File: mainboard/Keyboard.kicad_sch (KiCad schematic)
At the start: 111 parts, among them J10 Cassette, J11 Joystick, J12 Keyboard, Q3 TIS92, Q4 TIS92, Q5 TIS92, Q6 TIS92, Q7 TIS92, Q8 TIS92, Q9 TIS92, U40 TMS9901, U41 RC4558, U42 74LS156, U43 TIL119, U44 TIL119

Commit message: PCB routed
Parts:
- L13, L14, L15, L16, L17, L18, L19, L20, L21, L22: footprint Resistor_THT:R_Axial_DIN0207_L6.3mm_D2.5mm_P15.24mm_Horizontal -> Resistor_THT:R_Axial_DIN0207_L6.3mm_D2.5mm_P7.62mm_Horizontal
- Q3, Q4, Q5, Q6, Q7, Q8, Q9: footprint (none) -> Package_TO_SOT_THT:TO-92_HandSolder
- U39: renamed from U40; footprint Package_DIP:DIP-40_W15.24mm_LongPads -> Package_DIP:DIP-40_W15.24mm_Socket_LongPads
- U40: renamed from U41; footprint Package_DIP:DIP-8_W7.62mm_LongPads -> Package_DIP:DIP-8_W7.62mm_Socket_LongPads
- U41: renamed from U42; footprint Package_DIP:DIP-16_W7.62mm_LongPads -> Package_DIP:DIP-16_W7.62mm_Socket_LongPads
- U42: renamed from U43; footprint (none) -> Package_DIP:DIP-6_W7.62mm_Socket_LongPads
- U43: renamed from U44; footprint (none) -> Package_DIP:DIP-6_W7.62mm_Socket_LongPads
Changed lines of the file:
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@@
   (symbol (lib_id "TI-Customs:TMS9901") (at 69.85 86.36 0) (unit 1)
     (in_bom yes) (on_board yes)
-    (property "Reference" "U40" (id 0) (at 81.28 57.15 0)
+    (property "Reference" "U39" (id 0) (at 81.28 57.15 0)
       (effects (font (size 1.524 1.524)) (justify right))
     )
@@
       (effects (font (size 1.524 1.524)))
     )
-    (property "Footprint" "Package_DIP:DIP-40_W15.24mm_LongPads" (id 2) (at 69.85 86.36 0)
+    (property "Footprint" "Package_DIP:DIP-40_W15.24mm_Socket_LongPads" (id 2) (at 69.85 86.36 0)
       (effects (font (size 1.524 1.524)) hide)
     )
@@
       (effects (font (size 1.27 1.27)) (justify left))
     )
-    (property "Footprint" "" (id 2) (at 189.23 53.975 0)
+    (property "Footprint" "Package_TO_SOT_THT:TO-92_HandSolder" (id 2) (at 189.23 53.975 0)
       (effects (font (size 1.27 1.27) italic) (justify left) hide)
     )
@@
   (symbol (lib_id "Console-rescue:TIL111") (at 210.82 52.07 0) (unit 1)
     (in_bom yes) (on_board yes)
-    (property "Reference" "U44" (id 0) (at 210.82 49.53 0)
+    (property "Reference" "U43" (id 0) (at 210.82 49.53 0)
       (effects (font (size 1.778 1.778)))
     )
@@
       (effects (font (size 1.778 1.778)))
     )
-    (property "Footprint" "" (id 2) (at 210.82 52.07 0)
+    (property "Footprint" "Package_DIP:DIP-6_W7.62mm_Socket_LongPads" (id 2) (at 210.82 52.07 0)
       (effects (font (size 1.524 1.524)) hide)
     )
@@
       (effects (font (size 1.27 1.27)) (justify left))
     )
-    (property "Footprint" "" (id 2) (at 231.14 53.975 0)
+    (property "Footprint" "Package_TO_SOT_THT:TO-92_HandSolder" (id 2) (at 231.14 53.975 0)
       (effects (font (size 1.27 1.27) italic) (justify left) hide)
     )
@@
       (effects (font (size 1.27 1.27)) (justify left))
     )
-    (property "Footprint" "" (id 2) (at 189.23 36.195 0)
+    (property "Footprint" "Package_TO_SOT_THT:TO-92_HandSolder" (id 2) (at 189.23 36.195 0)
       (effects (font (size 1.27 1.27) italic) (justify left) hide)
     )
@@
   (symbol (lib_id "Console-rescue:TIL111") (at 210.82 34.29 0) (unit 1)
     (in_bom yes) (on_board yes)
-    (property "Reference" "U43" (id 0) (at 210.82 31.75 0)
+    (property "Reference" "U42" (id 0) (at 210.82 31.75 0)
       (effects (font (size 1.778 1.778)))
     )
@@
       (effects (font (size 1.778 1.778)))
     )
-    (property "Footprint" "" (id 2) (at 210.82 34.29 0)
+    (property "Footprint" "Package_DIP:DIP-6_W7.62mm_Socket_LongPads" (id 2) (at 210.82 34.29 0)
       (effects (font (size 1.524 1.524)) hide)
     )
@@
       (effects (font (size 1.27 1.27)) (justify left))
     )
-    (property "Footprint" "" (id 2) (at 231.14 36.195 0)
+    (property "Footprint" "Package_TO_SOT_THT:TO-92_HandSolder" (id 2) (at 231.14 36.195 0)
       (effects (font (size 1.27 1.27) italic) (justify left) hide)
     )
@@
       (effects (font (size 1.27 1.27)) (justify left))
     )
-    (property "Footprint" "Resistor_THT:R_Axial_DIN0207_L6.3mm_D2.5mm_P15.24mm_Horizontal" (id 2) (at 245.11 49.53 0)
+    (property "Footprint" "Resistor_THT:R_Axial_DIN0207_L6.3mm_D2.5mm_P7.62mm_Horizontal" (id 2) (at 245.11 49.53 0)
       (effects (font (size 1.524 1.524)) hide)
     )
@@
       (effects (font (size 1.27 1.27)) (justify left))
     )
-    (property "Footprint" "Resistor_THT:R_Axial_DIN0207_L6.3mm_D2.5mm_P15.24mm_Horizontal" (id 2) (at 245.11 31.75 0)
+    (property "Footprint" "Resistor_THT:R_Axial_DIN0207_L6.3mm_D2.5mm_P7.62mm_Horizontal" (id 2) (at 245.11 31.75 0)
       (effects (font (size 1.524 1.524)) hide)
     )
@@
       (effects (font (size 1.27 1.27)) (justify left))
     )
-    (property "Footprint" "Resistor_THT:R_Axial_DIN0207_L6.3mm_D2.5mm_P15.24mm_Horizontal" (id 2) (at 231.14 20.32 0)
+    (property "Footprint" "Resistor_THT:R_Axial_DIN0207_L6.3mm_D2.5mm_P7.62mm_Horizontal" (id 2) (at 231.14 20.32 0)
       (effects (font (size 1.524 1.524)) hide)
     )
@@
       (effects (font (size 1.27 1.27)) (justify left))
     )
-    (property "Footprint" "Resistor_THT:R_Axial_DIN0207_L6.3mm_D2.5mm_P15.24mm_Horizontal" (id 2) (at 240.03 22.86 0)
+    (property "Footprint" "Resistor_THT:R_Axial_DIN0207_L6.3mm_D2.5mm_P7.62mm_Horizontal" (id 2) (at 240.03 22.86 0)
       (effects (font (size 1.524 1.524)) hide)
     )
@@
   (symbol (lib_id "74xx:74LS156") (at 115.57 149.86 0) (unit 1)
     (in_bom yes) (on_board yes)
-    (property "Reference" "U42" (id 0) (at 114.3 146.05 0)
+    (property "Reference" "U41" (id 0) (at 114.3 146.05 0)
       (effects (font (size 1.524 1.524)))
     )
@@
       (effects (font (size 1.524 1.524)))
     )
-    (property "Footprint" "Package_DIP:DIP-16_W7.62mm_LongPads" (id 2) (at 115.57 149.86 0)
+    (property "Footprint" "Package_DIP:DIP-16_W7.62mm_Socket_LongPads" (id 2) (at 115.57 149.86 0)
       (effects (font (size 1.524 1.524)) hide)
     )
@@
       (effects (font (size 1.27 1.27)) (justify left))
     )
-    (property "Footprint" "" (id 2) (at 154.94 53.975 0)
+    (property "Footprint" "Package_TO_SOT_THT:TO-92_HandSolder" (id 2) (at 154.94 53.975 0)
       (effects (font (size 1.27 1.27) italic) (justify left) hide)
     )
@@
     )
     (property "Value" "6.8µH" (id 1) (at 154.94 140.97 90))
-    (property "Footprint" "Resistor_THT:R_Axial_DIN0207_L6.3mm_D2.5mm_P15.24mm_Horizontal" (id 2) (at 154.94 139.7 0)
+    (property "Footprint" "Resistor_THT:R_Axial_DIN0207_L6.3mm_D2.5mm_P7.62mm_Horizontal" (id 2) (at 154.94 139.7 0)
       (effects (font (size 1.524 1.524)) hide)
     )
@@
     )
     (property "Value" "6.8µH" (id 1) (at 167.64 143.51 90))
-    (property "Footprint" "Resistor_THT:R_Axial_DIN0207_L6.3mm_D2.5mm_P15.24mm_Horizontal" (id 2) (at 167.64 142.24 0)
+    (property "Footprint" "Resistor_THT:R_Axial_DIN0207_L6.3mm_D2.5mm_P7.62mm_Horizontal" (id 2) (at 167.64 142.24 0)
       (effects (font (size 1.524 1.524)) hide)
     )
@@
     )
     (property "Value" "6.8µH" (id 1) (at 154.94 153.67 90))
-    (property "Footprint" "Resistor_THT:R_Axial_DIN0207_L6.3mm_D2.5mm_P15.24mm_Horizontal" (id 2) (at 154.94 152.4 0)
+    (property "Footprint" "Resistor_THT:R_Axial_DIN0207_L6.3mm_D2.5mm_P7.62mm_Horizontal" (id 2) (at 154.94 152.4 0)
       (effects (font (size 1.524 1.524)) hide)
     )
@@
     )
     (property "Value" "6.8µH" (id 1) (at 167.64 156.21 90))
-    (property "Footprint" "Resistor_THT:R_Axial_DIN0207_L6.3mm_D2.5mm_P15.24mm_Horizontal" (id 2) (at 167.64 154.94 0)
+    (property "Footprint" "Resistor_THT:R_Axial_DIN0207_L6.3mm_D2.5mm_P7.62mm_Horizontal" (id 2) (at 167.64 154.94 0)
       (effects (font (size 1.524 1.524)) hide)
     )
@@
     )
     (property "Value" "6.8µH" (id 1) (at 180.34 158.75 90))
-    (property "Footprint" "Resistor_THT:R_Axial_DIN0207_L6.3mm_D2.5mm_P15.24mm_Horizontal" (id 2) (at 180.34 157.48 0)
+    (property "Footprint" "Resistor_THT:R_Axial_DIN0207_L6.3mm_D2.5mm_P7.62mm_Horizontal" (id 2) (at 180.34 157.48 0)
       (effects (font (size 1.524 1.524)) hide)
     )
@@
     )
     (property "Value" "6.8µH" (id 1) (at 193.04 161.29 90))
-    (property "Footprint" "Resistor_THT:R_Axial_DIN0207_L6.3mm_D2.5mm_P15.24mm_Horizontal" (id 2) (at 193.04 160.02 0)
+    (property "Footprint" "Resistor_THT:R_Axial_DIN0207_L6.3mm_D2.5mm_P7.62mm_Horizontal" (id 2) (at 193.04 160.02 0)
       (effects (font (size 1.524 1.524)) hide)
     )
@@
       (effects (font (size 1.27 1.27)) (justify left))
     )
-    (property "Footprint" "" (id 2) (at 207.01 118.745 0)
+    (property "Footprint" "Package_TO_SOT_THT:TO-92_HandSolder" (id 2) (at 207.01 118.745 0)
       (effects (font (size 1.27 1.27) italic) (justify left) hide)
     )
@@
       (effects (font (size 1.27 1.27)) (justify left))
     )
-    (property "Footprint" "" (id 2) (at 180.34 118.745 0)
+    (property "Footprint" "Package_TO_SOT_THT:TO-92_HandSolder" (id 2) (at 180.34 118.745 0)
       (effects (font (size 1.27 1.27) italic) (justify left) hide)
     )
@@
   (symbol (lib_id "Console-rescue:LM358") (at 135.89 33.02 180) (unit 2)
     (in_bom yes) (on_board yes)
-    (property "Reference" "U41" (id 0) (at 135.89 33.02 0)
+    (property "Reference" "U40" (id 0) (at 135.89 33.02 0)
       (effects (font (size 1.524 1.524)))
     )
@@
       (effects (font (size 1.524 1.524)) (justify right))
     )
-    (property "Footprint" "Package_DIP:DIP-8_W7.62mm_LongPads" (id 2) (at 135.89 33.02 0)
+    (property "Footprint" "Package_DIP:DIP-8_W7.62mm_Socket_LongPads" (id 2) (at 135.89 33.02 0)
       (effects (font (size 1.524 1.524)) hide)
     )
@@
   (symbol (lib_id "Console-rescue:LM358") (at 115.57 43.18 0) (mirror y) (unit 1)
     (in_bom yes) (on_board yes)
-    (property "Reference" "U41" (id 0) (at 115.57 43.18 0)
+    (property "Reference" "U40" (id 0) (at 115.57 43.18 0)
       (effects (font (size 1.524 1.524)))
     )
@@
       (effects (font (size 1.524 1.524)) (justify right))
     )
-    (property "Footprint" "Package_DIP:DIP-8_W7.62mm_LongPads" (id 2) (at 115.57 43.18 0)
-      (effects (font (size 1.524 1.524)) hide)
-    )
+    (property "Footprint" "Package_DIP:DIP-8_W7.62mm_Socket_LongPads" (id 2) (at 115.57 43.18 0)
+      (effects (font (size 1.524 1.524)) hide)
+    )

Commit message: unicorn work
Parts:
- removed J12: Keyboard, Connector_PinHeader_2.54mm:PinHeader_1x15_P2.54mm_Vertical, symbol Console-rescue:CONN_01X15
- added J12: Keyboard, symbol Connector_Generic:Conn_01x18
- renumbered C62 to C54, C63 to C55, C64 to C56, C65 to C57, C66 to C58, C67 to C59, C68 to C60, C69 to C61, C70 to C62, C71 to C63, C72 to C64, C73 to C65, C74 to C66, C75 to C67, C76 to C68, C77 to C69, C78 to C70, C79 to C71, C80 to C72, C81 to C73, C82 to C74, C83 to C75, C84 to C76, C85 to C77, C86 to C78, C87 to C79, C88 to C80, C89 to C81, C90 to C82, C91 to C83, C92 to C84, C93 to C85, C94 to C86, C95 to C87, C96 to C88, R39 to R35, R40 to R36, R41 to R37, R42 to R38, R43 to R39, R44 to R40, R45 to R41, R46 to R42, R47 to R43, R48 to R44, R49 to R45, R50 to R46, R51 to R47, R52 to R48, R53 to R49, R54 to R50, R55 to R51, R56 to R52, R57 to R53, R58 to R54, R59 to R55, R60 to R56, R61 to R57, R62 to R58, R63 to R59, R64 to R60, R65 to R61, R66 to R62, R67 to R63, R68 to R64, R69 to R65, R70 to R66, R71 to R67, R72 to R68, R73 to R69, R74 to R70, R75 to R71, R76 to R72, R77 to R73, R78 to R74, R79 to R75, R80 to R76, R81 to R77, R82 to R78, R83 to R79, R84 to R80, R85 to R81, R86 to R82, R87 to R83, R88 to R84, U39 to U35, U40 to U36, U41 to U37, U42 to U38, U43 to U39
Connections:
- net +5V: now also J12.17 (Pin_17)
- net GND: now also J12.16 (Pin_16)
- net ~{RESET}: now also J12.18 (Pin_18)
- net at L13.2: now also J12.9 (Pin_9)
- net at L15.2: now also J12.8 (Pin_8)
- net at L14.2: now also J12.12 (Pin_12)
- net at L16.2: now also J12.13 (Pin_13)
- net at L17.2: now also J12.14 (Pin_14)
- net at L18.2: now also J12.15 (Pin_15)
- net at J11.9, R68.1: now also J12.1 (Pin_1)
- net at R78.1: now also J12.10 (Pin_10)
- net at R80.1: now also J12.11 (Pin_11)
- net at J11.8, R70.1: now also J12.2 (Pin_2)
- net at R76.1: now also J12.3 (Pin_3)
- net at J11.5, R66.1: now also J12.4 (Pin_4)
- net at J11.4, R64.1: now also J12.5 (Pin_5)
- net at R83.1: now also J12.6 (Pin_6)
- net at J11.3, R72.1: now also J12.7 (Pin_7)
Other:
- moved on the sheet: C54, C55, C56, C57, C58, C59, C60, C61, C62, C63, C64, C65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

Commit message: unicorn work
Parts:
- J12: footprint (none) -> Connector_PinHeader_2.54mm:PinHeader_1x18_P2.54mm_Vertical
- renumbered C54 to C62, C55 to C63, C56 to C64, C57 to C65, C58 to C66, C59 to C67, C60 to C68, C61 to C69, C62 to C70, C63 to C71, C64 to C72, C65 to C73, C66 to C74, C67 to C75, C68 to C76, C69 to C77, C70 to C78, C71 to C79, C72 to C80, C73 to C81, C74 to C82, C75 to C83, C76 to C84, C77 to C85, C78 to C86, C79 to C87, C80 to C88, C81 to C89, C82 to C90, C83 to C91, C84 to C92, C85 to C93, C86 to C94, C87 to C95, C88 to C96

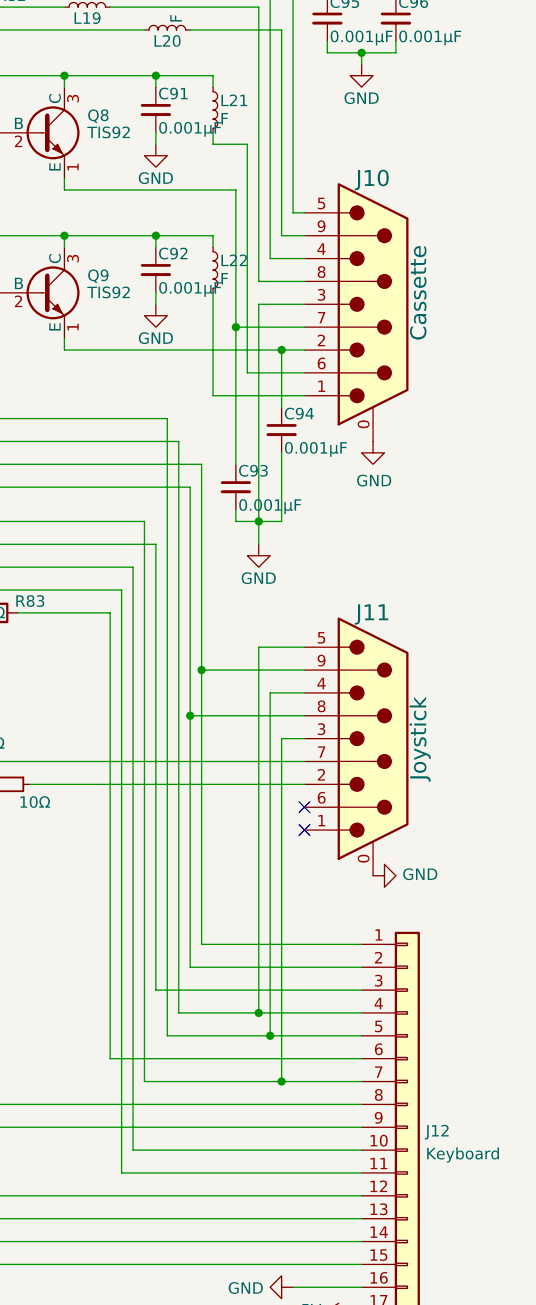
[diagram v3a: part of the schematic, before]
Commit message: Shrink PCB
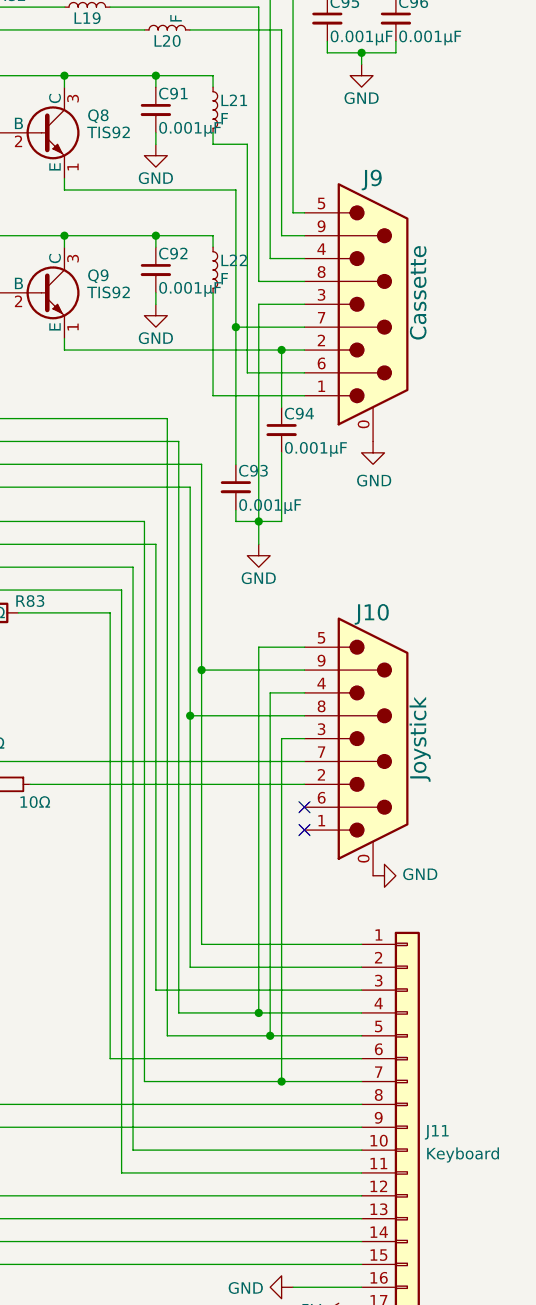
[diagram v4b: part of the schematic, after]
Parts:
- renumbered J11 to J10, J12 to J11, J10 to J9
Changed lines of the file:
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@@
   (symbol (lib_id "Connector:DB9_Male_MountingHoles") (at 254 97.79 0) (unit 1)
     (in_bom yes) (on_board yes)
-    (property "Reference" "J11" (id 0) (at 254 83.82 0)
+    (property "Reference" "J10" (id 0) (at 254 83.82 0)
       (effects (font (size 1.778 1.778)))
     )
@@
   (symbol (lib_id "Connector:DB9_Male_MountingHoles") (at 254 49.53 0) (unit 1)
     (in_bom yes) (on_board yes)
-    (property "Reference" "J10" (id 0) (at 254 35.56 0)
+    (property "Reference" "J9" (id 0) (at 254 35.56 0)
       (effects (font (size 1.778 1.778)))
     )
@@
   (symbol (lib_id "Connector_Generic:Conn_01x18") (at 257.81 140.97 0) (unit 1)
     (in_bom yes) (on_board yes) (fields_autoplaced)
-    (property "Reference" "J12" (id 0) (at 259.842 141.4053 0)
-      (effects (font (size 1.27 1.27)) (justify left))
-    )
+    (property "Reference" "J11" (id 0) (at 259.842 141.4053 0)
+      (effects (font (size 1.27 1.27)) (justify left))
+    )

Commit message: hardware updates
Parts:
- renumbered L13 to L12, L14 to L13, L15 to L14, L16 to L15, L17 to L16, L18 to L17, L19 to L18, L20 to L19, L21 to L20, L22 to L21, R35 to R34, R36 to R35, R37 to R36, R38 to R37, R39 to R38, R40 to R39, R41 to R40, R42 to R41, R43 to R42, R44 to R43, R45 to R44, R46 to R45, R47 to R46, R48 to R47, R49 to R48, R50 to R49, R51 to R50, R52 to R51, R53 to R52, R54 to R53, R55 to R54, R56 to R55, R57 to R56, R58 to R57, R59 to R58, R60 to R59, R61 to R60, R62 to R61, R63 to R62, R64 to R63, R65 to R64, R66 to R65, R67 to R66, R68 to R67, R69 to R68, R70 to R69, R71 to R70, R72 to R71, R73 to R72, R74 to R73, R75 to R74, R76 to R75, R77 to R76, R78 to R77, R79 to R78, R80 to R79, R81 to R80, R82 to R81, R83 to R82, R84 to R83

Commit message: Add BOM
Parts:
- J10, J9: footprint Connector_Dsub:DSUB-9_Male_Horizontal_P2.77x2.84mm_EdgePinOffset14.56mm_Housed_MountingHolesOffset8.20mm -> Connector_Dsub:DSUB-9_Female_Horizontal_P2.77x2.84mm_EdgePinOffset4.94mm_Housed_MountingHolesOffset7.48mm
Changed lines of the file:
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@@
   (title_block
     (title "TI-99/22")
-    (date "2022-10-11")
-    (rev "0.76")
+    (date "2022-11-19")
+    (rev "0.9")
     (company "Dan Werner - https://github.com/danwerner21/ti99_22")
     (comment 1 "Schematic for Keyboard, Joystick and Cassette port.")
@@
       (effects (font (size 1.778 1.778)))
     )
-    (property "Footprint" "Connector_Dsub:DSUB-9_Male_Horizontal_P2.77x2.84mm_EdgePinOffset14.56mm_Housed_MountingHolesOffset8.20mm" (id 2) (at 254 97.79 0)
+    (property "Footprint" "Connector_Dsub:DSUB-9_Female_Horizontal_P2.77x2.84mm_EdgePinOffset4.94mm_Housed_MountingHolesOffset7.48mm" (id 2) (at 254 97.79 0)
       (effects (font (size 1.524 1.524)) hide)
     )
@@
       (effects (font (size 1.778 1.778)))
     )
-    (property "Footprint" "Connector_Dsub:DSUB-9_Male_Horizontal_P2.77x2.84mm_EdgePinOffset14.56mm_Housed_MountingHolesOffset8.20mm" (id 2) (at 254 49.53 0)
+    (property "Footprint" "Connector_Dsub:DSUB-9_Female_Horizontal_P2.77x2.84mm_EdgePinOffset4.94mm_Housed_MountingHolesOffset7.48mm" (id 2) (at 254 49.53 0)
       (effects (font (size 1.524 1.524)) hide)
     )

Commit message: PCB cleanup
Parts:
- C62, C63, C64, C65, C66, C67, C68, C69, C70, C71, C73, C74, C75, C76, C79, C80, C81, C82, C83, C88, C89, C90, C91, C92, C93, C94, C95, C96: symbol TI-Customs:C_Small -> Device:C
- C72: renamed from C78; symbol TI-Customs:C_Small -> Device:C
- C77: renamed from C72; symbol TI-Customs:C_Small -> Device:C
- C78: renamed from C77; symbol TI-Customs:C_Small -> Device:C
- C84: renamed from C87; symbol TI-Customs:C_Small -> Device:C
- C85: renamed from C84; symbol TI-Customs:C_Small -> Device:C
- C86: renamed from C85; symbol TI-Customs:C_Small -> Device:C
- C87: renamed from C86; symbol TI-Customs:C_Small -> Device:C
- CR4: symbol Console-rescue:D -> Device:D
- L12, L13, L14, L15, L16, L17, L18, L19, L20, L21: symbol Console-rescue:L_Small -> Device:L_Small
- Q3, Q4, Q5, Q6, Q7, Q8, Q9: symbol Console-rescue:S8050 -> Device:Q_NPN_EBC
- R34, R40, R41, R42, R43, R44, R45, R46, R47, R48, R50, R51, R52, R53, R54, R55, R56, R63, R65, R67, R69, R71, R75, R77, R79, R82: symbol Console-rescue:R -> Device:R
- R35, R36, R37, R38, R39, R49, R57, R58, R59, R60, R61, R62, R64, R66, R68, R70, R72, R73, R74, R76, R78, R80, R81, R83: symbol Console-rescue:R_Small -> Device:R_Small
- U21: renamed from U36; symbol Console-rescue:LM358 -> Amplifier_Operational:RC4558
- U36: renamed from U35; symbol TI-Customs:TMS9901 -> Werner_custom:TMS9901
- U38, U39: symbol Console-rescue:TIL111 -> Werner_custom:TIL119
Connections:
- net +5V: no longer U21.8 (V+), U21.8 (V+)
- net -5V: no longer U21.4 (V-), U21.4 (V-)
- net at R48.1, R82.2, U36.20 (P5): now also C78.1; no longer C72.1
- net at R46.1, R77.2, U36.32 (P13/~{INT9}): now also C77.1; no longer C78.1
- net at R45.1, R75.2, U36.33 (P14/~{INT8}): now also C72.1; no longer C77.1
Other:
- moved on the sheet: C62, C65, C66, C68, C69, C70, C71, C72, C73, C74, C75, C76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
